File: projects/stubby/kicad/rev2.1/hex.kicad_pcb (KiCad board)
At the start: 2 copper layers, 49.5 x 49.5 mm, 72 parts, among them IC1 ATMEGA1284-A, P1 BATT (4.8V-6V), P10 CONN_4, P11 CONN_4, P2 PROG, P3 CONN_10, P4 CONN_6, P5 CONN_13, P6 CONN_6, P7 CONN_1, P8 CONN_6, P9 CONN_2, SW1 DPDT, SW2 SW_PUSH, U1 HMC5883L, X1 CRYSTAL

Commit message: Move some test points around a bit
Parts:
- added 1PIN: P***, 1pin, F.Cu at (84.3, 45.7)
- moved 1PIN 26.7 mm to (36.3, 46.0)
- moved 1PIN 1.27 mm to (36.2, 49.5)
- moved 1PIN 1.27 mm to (84.5, 49.5)
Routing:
- net GND: track 316.4 -> 318.2 mm
- net /I2C_SCL: vias 3 -> 4
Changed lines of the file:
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@@
-(kicad_pcb (version 3) (host pcbnew "(2013-dec-23)-stable")
+(kicad_pcb (version 3) (host pcbnew "(2014-01-10 BZR 4027)-stable")
   (general
     (links 0)
     (no_connects 0)
-    (area 23.115001 8.662599 86.992177 70.645)
+    (area 23.115001 7.392599 87.857401 70.645)
     (thickness 1.6)
-    (drawings 83)
-    (tracks 893)
+    (drawings 84)
+    (tracks 896)
     (zones 0)
-    (modules 72)
+    (modules 73)
     (nets 62)
   )
@@
     (add_net N-000007)
   )
+  (module 1pin (layer F.Cu)
+    (at 84.328 45.72)
+    (descr "module 1 pin (ou trou mecanique de percage)")
+    (tags DEV)
+    (path 1pin)
+    (fp_text reference 1PIN (at 0 -3.048) (layer F.SilkS) hide
+      (effects (font (size 1.016 1.016) (thickness 0.254)))
+    )
+    (fp_text value P*** (at 0 2.794) (layer F.SilkS) hide
+      (effects (font (size 1.016 1.016) (thickness 0.254)))
+    )
+    (pad 1 thru_hole circle (at 0 0) (size 1.27 1.27) (drill 1.016)
+      (layers *.Cu *.Mask F.SilkS)
+      (net 48 GND)
+    )
+  )
   (module C1V8 (layer F.Cu)
     (at 39.37 16.51 180)
@@
   )
   (module 1pin (layer F.Cu)
-    (at 36.322 19.304)
+    (at 36.322 45.974)
     (descr "module 1 pin (ou trou mecanique de percage)")
     (tags DEV)
@@
   )
   (module 1pin (layer F.Cu)
-    (at 36.195 48.26)
+    (at 36.195 49.53)
     (descr "module 1 pin (ou trou mecanique de percage)")
     (tags DEV)
@@
   )
   (module 1pin (layer F.Cu)
-    (at 84.455 48.26)
+    (at 84.455 49.53)
     (descr "module 1 pin (ou trou mecanique de percage)")
     (tags DEV)
@@
     )
   )
+  (gr_text GND (at 82.804 45.72) (layer F.SilkS)
+    (effects (font (size 0.508 0.508) (thickness 0.127)))
+  )
   (gr_line (start 81.915 57.15) (end 83.82 57.15) (angle 90) (layer Edge.Cuts) (width 0.1))
   (gr_line (start 81.915 55.88) (end 82.55 55.88) (angle 90) (layer Edge.Cuts) (width 0.1))
@@
     (effects (font (size 0.508 0.508) (thickness 0.127)))
   )
-  (gr_text GND (at 37.846 19.304) (layer F.SilkS)
+  (gr_text GND (at 37.846 45.974) (layer F.SilkS)
     (effects (font (size 0.508 0.508) (thickness 0.127)))
   )
@@
   (segment (start 53.975 48.26) (end 55.245 48.26) (width 0.254) (layer B.Cu) (net 12))
   (segment (start 50.8 51.435) (end 53.975 48.26) (width 0.254) (layer B.Cu) (net 12))
-  (segment (start 82.55 46.99) (end 83.82 45.72) (width 0.254) (layer B.Cu) (net 13))
-  (segment (start 83.82 37.465) (end 83.82 37.338) (width 0.254) (layer B.Cu) (net 13))
-  (segment (start 83.82 45.72) (end 83.82 37.465) (width 0.254) (layer B.Cu) (net 13))
-  (segment (start 74.93 54.61) (end 74.93 53.975) (width 0.254) (layer B.Cu) (net 13))
-  (segment (start 83.82 37.338) (end 83.82 37.338) (width 0.254) (layer B.Cu) (net 13))
-  (segment (start 83.82 37.338) (end 84.328 36.83) (width 0.254) (layer B.Cu) (net 13))
-  (segment (start 82.55 52.705) (end 82.55 46.99) (width 0.254) (layer B.Cu) (net 13))
-  (segment (start 81.915 53.34) (end 82.55 52.705) (width 0.254) (layer B.Cu) (net 13))
-  (segment (start 75.565 53.34) (end 81.915 53.34) (width 0.254) (layer B.Cu) (net 13))
+  (segment (start 83.185 38.1) (end 83.185 37.973) (width 0.254) (layer F.Cu) (net 13))
   (segment (start 74.93 53.975) (end 75.565 53.34) (width 0.254) (layer B.Cu) (net 13))
+  (segment (start 75.565 53.34) (end 81.915 53.34) (width 0.254) (layer B.Cu) (net 13))
+  (segment (start 81.915 53.34) (end 82.55 52.705) (width 0.254) (layer B.Cu) (net 13))
+  (segment (start 82.55 46.863) (end 82.55 45.72) (width 0.254) (layer F.Cu) (net 13))
+  (segment (start 82.55 45.72) (end 83.185 45.085) (width 0.254) (layer F.Cu) (net 13))
+  (segment (start 83.185 45.085) (end 83.185 38.1) (width 0.254) (layer F.Cu) (net 13))
+  (via (at 82.55 46.863) (size 0.762) (layers F.Cu B.Cu) (net 13))
+  (segment (start 82.55 52.705) (end 82.55 46.863) (width 0.254) (layer B.Cu) (net 13))
+  (segment (start 83.185 37.973) (end 84.328 36.83) (width 0.254) (layer F.Cu) (net 13))
+  (segment (start 74.93 54.61) (end 74.93 53.975) (width 0.254) (layer B.Cu) (net 13) (status 80))
   (segment (start 74.93 54.61) (end 74.93 52.07) (width 0.254) (layer B.Cu) (net 13))
   (segment (start 75.45 51.55) (end 75.45 50.805) (width 0.254) (layer F.Cu) (net 13))
@@
   (segment (start 68.435786 49.674214) (end 68.435786 48.254274) (width 0.254) (layer F.Cu) (net 47))
   (segment (start 68.435786 48.254274) (end 66.836871 46.655359) (width 0.254) (layer F.Cu) (net 47))
+  (segment (start 84.328 45.72) (end 84.328 46.482) (width 0.254) (layer F.Cu) (net 48))
+  (segment (start 83.185 47.625) (end 80.645 47.625) (width 0.254) (layer F.Cu) (net 48))
+  (segment (start 84.328 46.482) (end 83.185 47.625) (width 0.254) (layer F.Cu) (net 48))
   (segment (start 63.1825 22.225) (end 63.1825 19.3675) (width 0.762) (layer F.Cu) (net 48))
   (segment (start 63.1825 19.3675) (end 65.405 17.145) (width 0.762) (layer F.Cu) (net 48))
@@
   (segment (start 60.325 20.955) (end 60.325 15.875) (width 1.27) (layer F.Cu) (net 48))
   (segment (start 60.96 15.24) (end 71.12 15.24) (width 1.27) (layer F.Cu) (net 48))
-  (segment (start 36.322 19.304) (end 37.084 19.304) (width 0.254) (layer F.Cu) (net 48))
-  (segment (start 37.084 19.304) (end 38.735 20.955) (width 0.254) (layer F.Cu) (net 48))
   (segment (start 46.99 27.94) (end 39.37 27.94) (width 0.254) (layer B.Cu) (net 48))
   (segment (start 38.735 28.575) (end 38.735 29.845) (width 0.254) (layer B.Cu) (net 48))
@@
   (segment (start 81.915 50.8) (end 81.915 53.975) (width 0.254) (layer F.Cu) (net 48))
   (segment (start 80.645 49.53) (end 81.915 50.8) (width 0.254) (layer F.Cu) (net 48))
-  (segment (start 80.645 46.355) (end 80.645 49.53) (width 0.254) (layer F.Cu) (net 48))
+  (segment (start 80.645 46.355) (end 80.645 47.625) (width 0.254) (layer F.Cu) (net 48))
+  (segment (start 80.645 47.625) (end 80.645 49.53) (width 0.254) (layer F.Cu) (net 48))
   (segment (start 81.915 45.085) (end 80.645 46.355) (width 0.254) (layer F.Cu) (net 48))
   (segment (start 77.47 54.61) (end 81.28 54.61) (width 0.254) (layer F.Cu) (net 48))

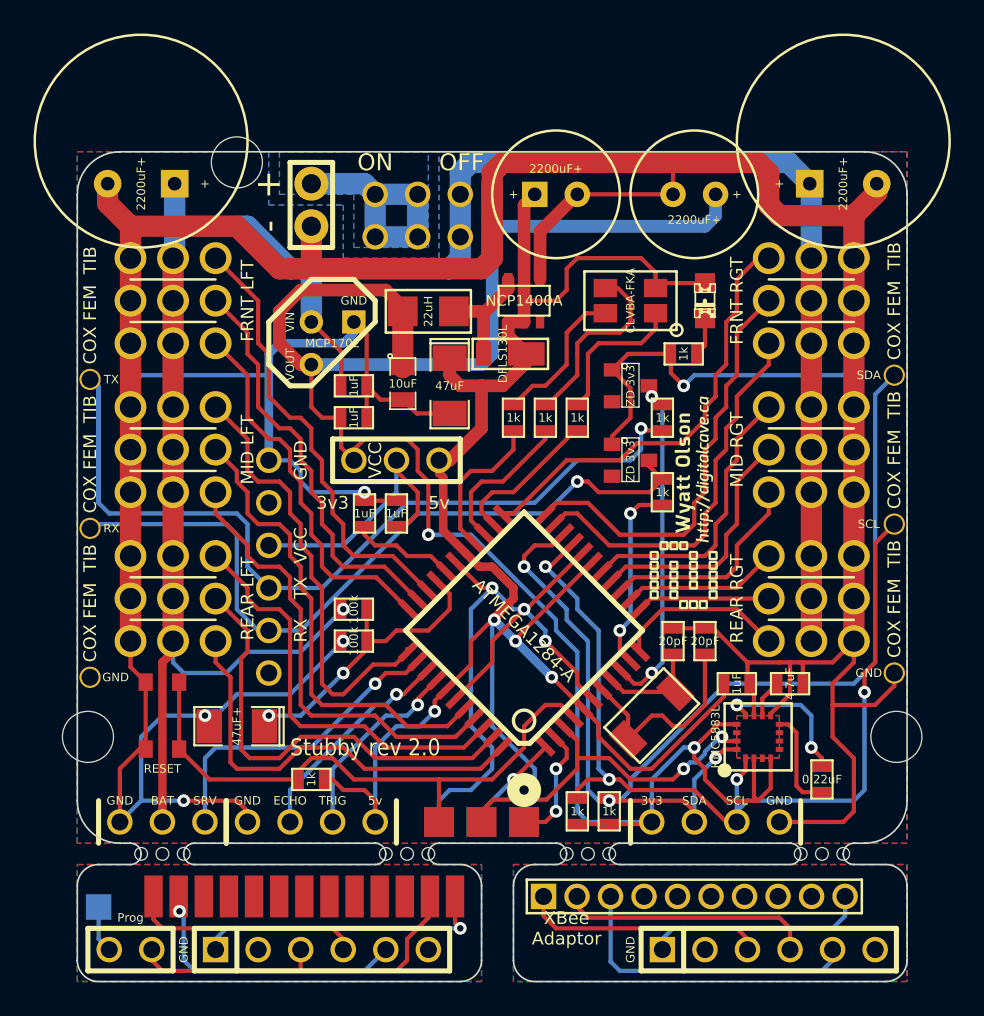
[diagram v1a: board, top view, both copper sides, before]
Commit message: Improve mounting holes and reset button; move some vias from underneath pads
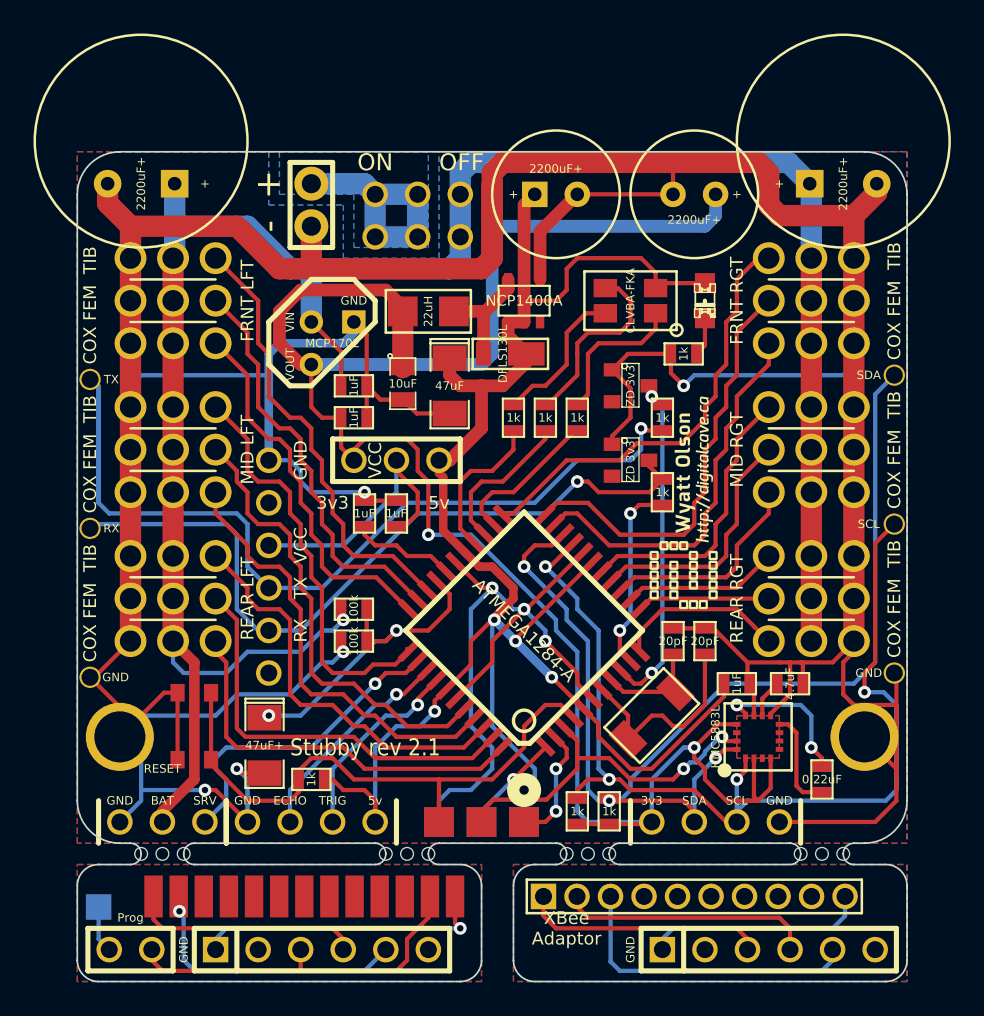
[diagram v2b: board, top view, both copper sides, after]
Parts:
- removed the 1PIN at (45.1, 15.2)
- moved SW2 2.01 mm to (42.5, 48.9)
- moved C10 2.01 mm to (46.7, 50.0), turned to 270 degrees
- moved 1PIN 1.91 mm to (38.1, 49.5)
- moved 1PIN 1.91 mm to (82.5, 49.5)
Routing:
- net GND: track 318.2 -> 333.1 mm
- net /I2C_SCL: track 57.2 -> 60.6 mm
- net /PWM13: track 26.9 -> 24.9 mm
- net /PWM12: track 25.7 -> 23.9 mm
- net /PWM08: track 26.6 -> 24.8 mm
- net /ADC_BATTERY_METER: track 17.8 -> 19.6 mm
- net +BATT: track 132.0 -> 133.3 mm
- net /PWM07: track 28.2 -> 27.4 mm
- net /PWM06: track 27.3 -> 26.5 mm
- net /PWM14: track 25.0 -> 24.3 mm
- net /RESET: track 35.0 -> 34.5 mm
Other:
- board text added: "Stubby rev 2.1"
- board text removed: "Stubby rev 2.0"

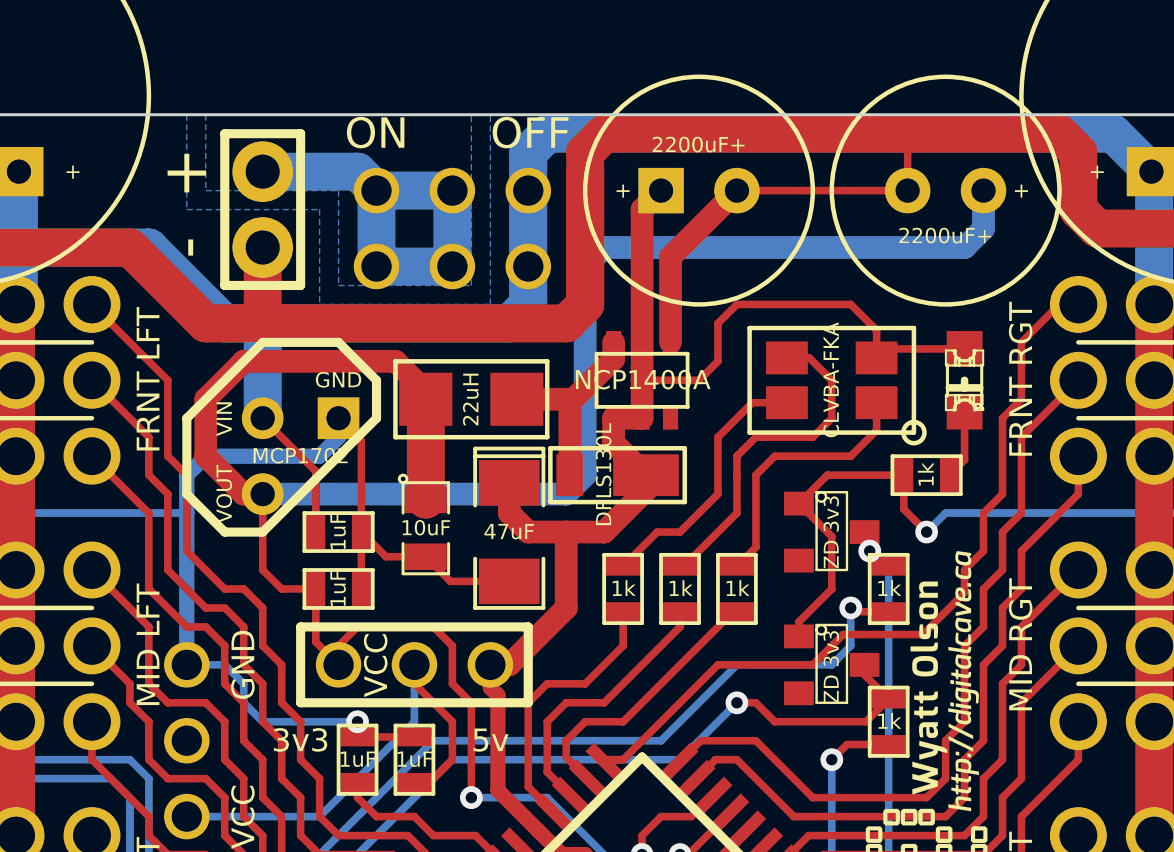
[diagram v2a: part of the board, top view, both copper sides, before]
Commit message: convert mcp1702 to sot23 form factor
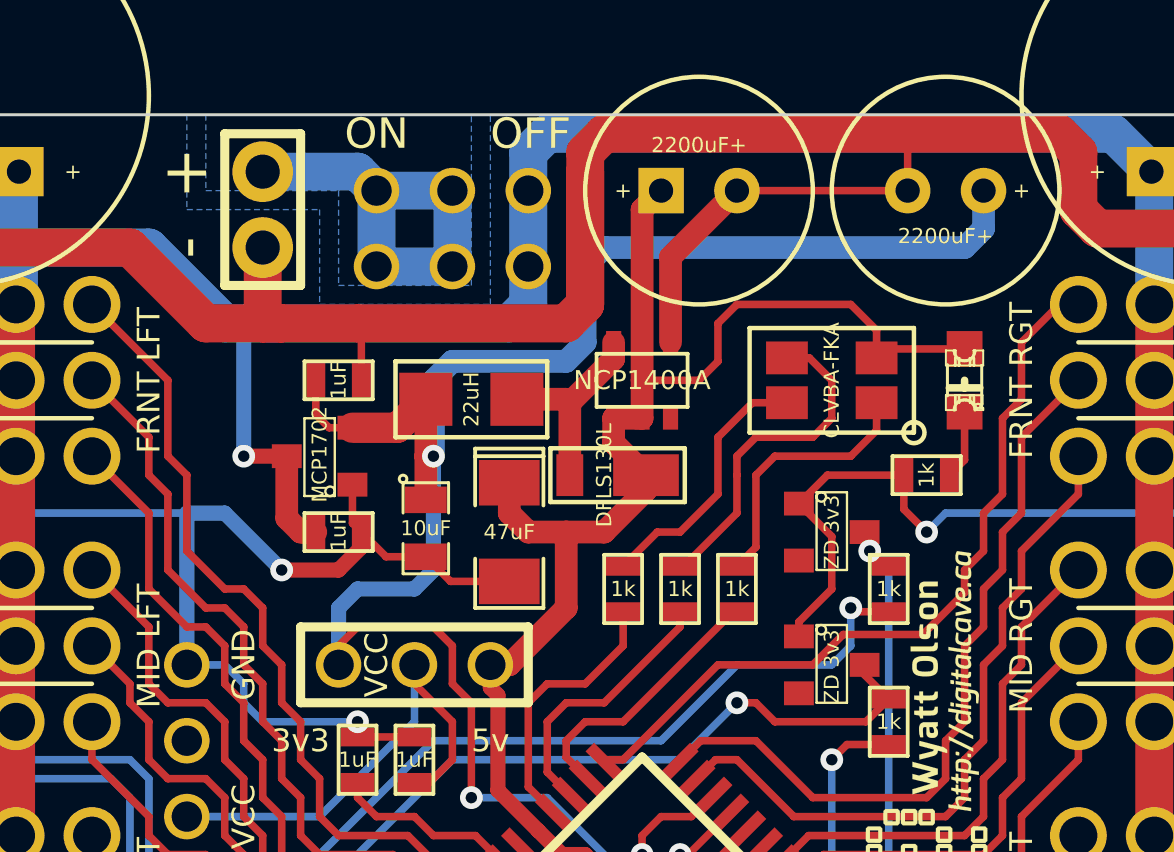
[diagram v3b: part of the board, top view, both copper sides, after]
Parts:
- VR1: footprint TO92 -> SOT23
- moved C2 6.98 mm to (52.1, 23.5)
- moved VR1 0.64 mm to (51.4, 26.0), turned to 90 degrees
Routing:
- net +3.3V: track 118.7 -> 106.1 mm, vias 2 -> 3
- net GND: track 333.1 -> 330.8 mm, vias 8 -> 9
- net +BATT: track 133.3 -> 134.7 mm, vias 1 -> 2
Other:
- board text removed: "VIN"
- board text removed: "VOUT"

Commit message: Changed to SMD capacitors for 3v3 and 5v reservoirs on 2.1... I am unsure of this change.  The SMD caps are more expensive and harder to place, and so I had to put one of them on the bottom of the board.  Will think more about this...
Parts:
- C1: footprint C1V7 -> c_elec_10x10
- C8: footprint C1V7 -> c_elec_10x10; moved to B.Cu
- moved C8 5.12 mm to (69.2, 17.8), turned to 180 degrees
- moved C1 3.24 mm to (69.2, 17.8)
- moved R1 2.29 mm to (73.0, 28.6), turned to 270 degrees
- moved D3 2.01 mm to (67.9, 25.4)
- moved D2 1.90 mm to (73.0, 25.4)
- moved ZD1 1.42 mm to (67.9, 29.8), turned to 180 degrees
- moved ZD2 1.42 mm to (67.9, 34.3), turned to 180 degrees
- moved C3 1.27 mm to (52.1, 29.8)
- moved R8 0.64 mm to (70.5, 35.6)
- moved VR1 0.64 mm to (51.4, 26.7)
- moved R9 0.63 mm to (70.5, 31.1)
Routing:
- net GND: track 330.8 -> 320.3 mm
- net +3.3V: track 106.1 -> 98.9 mm, vias 3 -> 4
- net /LED_BL_R: track 11.3 -> 7.20 mm
- net /AVR_RX: track 21.1 -> 18.4 mm
- net /LED_RD_R: track 8.90 -> 6.56 mm
- net /MODULE_TX: track 57.2 -> 58.4 mm
- net N-000002: track 2.34 -> 1.36 mm
- net +BATT: track 134.7 -> 135.7 mm
- net +5V: track 111.6 -> 110.6 mm, vias 4 -> 5
- net /PWM03: track 26.0 -> 25.3 mm
- net /LED_GR: track 9.20 -> 8.53 mm
- net /AVR_TX: track 11.4 -> 10.9 mm
